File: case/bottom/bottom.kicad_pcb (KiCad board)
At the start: 2 copper layers, 166.2 x 102.2 mm, 0 parts

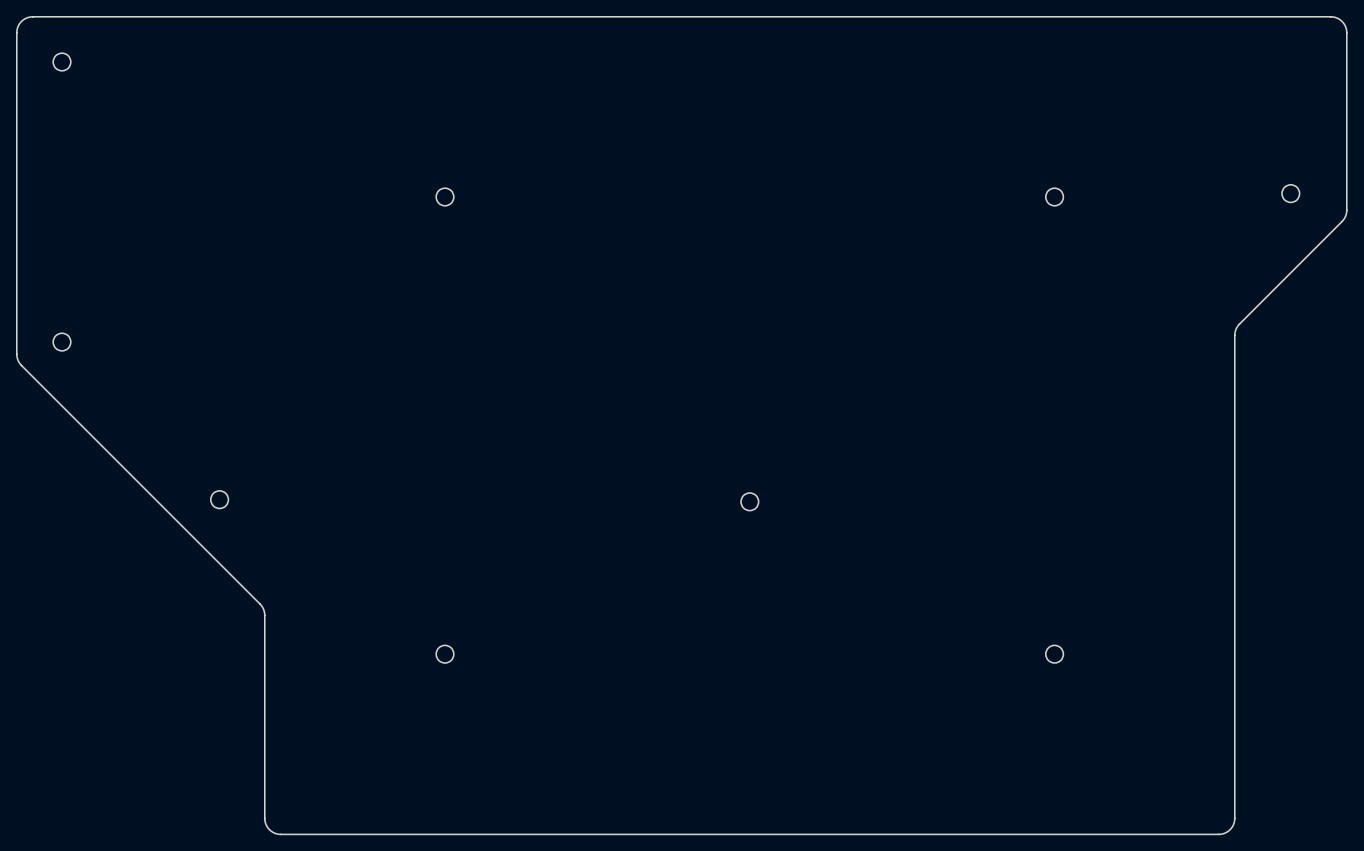
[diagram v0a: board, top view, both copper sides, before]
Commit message: Circles to holes
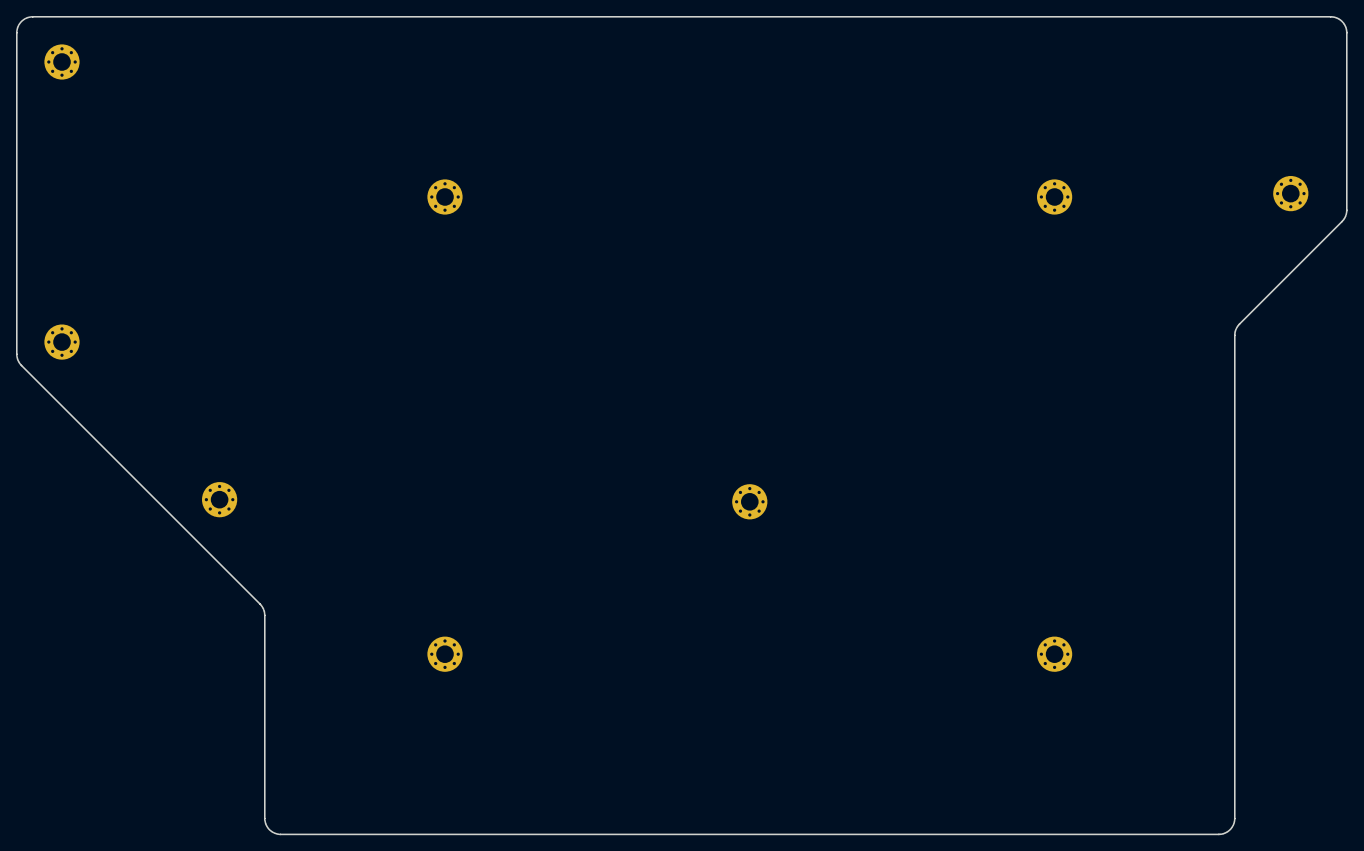
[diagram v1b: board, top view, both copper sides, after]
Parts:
- added REF**: MountingHole_2.2mm_M2_Pad_Via, MountingHole_2.2mm_M2_Pad_Via, F.Cu at (61.6, 42.6)
- added REF**: MountingHole_2.2mm_M2_Pad_Via, MountingHole_2.2mm_M2_Pad_Via, F.Cu at (61.6, 77.7)
- added REF**: MountingHole_2.2mm_M2_Pad_Via, MountingHole_2.2mm_M2_Pad_Via, F.Cu at (215.2, 59.1)
- added REF**: MountingHole_2.2mm_M2_Pad_Via, MountingHole_2.2mm_M2_Pad_Via, F.Cu at (185.7, 59.5)
- added REF**: MountingHole_2.2mm_M2_Pad_Via, MountingHole_2.2mm_M2_Pad_Via, F.Cu at (109.5, 59.5)
- added REF**: MountingHole_2.2mm_M2_Pad_Via, MountingHole_2.2mm_M2_Pad_Via, F.Cu at (109.5, 116.7)
- added REF**: MountingHole_2.2mm_M2_Pad_Via, MountingHole_2.2mm_M2_Pad_Via, F.Cu at (185.7, 116.7)
- added REF**: MountingHole_2.2mm_M2_Pad_Via, MountingHole_2.2mm_M2_Pad_Via, F.Cu at (147.6, 97.6)
- added REF**: MountingHole_2.2mm_M2_Pad_Via, MountingHole_2.2mm_M2_Pad_Via, F.Cu at (81.3, 97.4)
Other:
- outline, holes or cut-outs redrawn
